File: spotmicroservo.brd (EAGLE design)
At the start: 25.4 x 39.4 mm, 39 parts, among them J1 B4B-PH-SM4-TB(LF)(SN), J2 CON_HEADER_1X02-B2B-XH-A(LF)(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

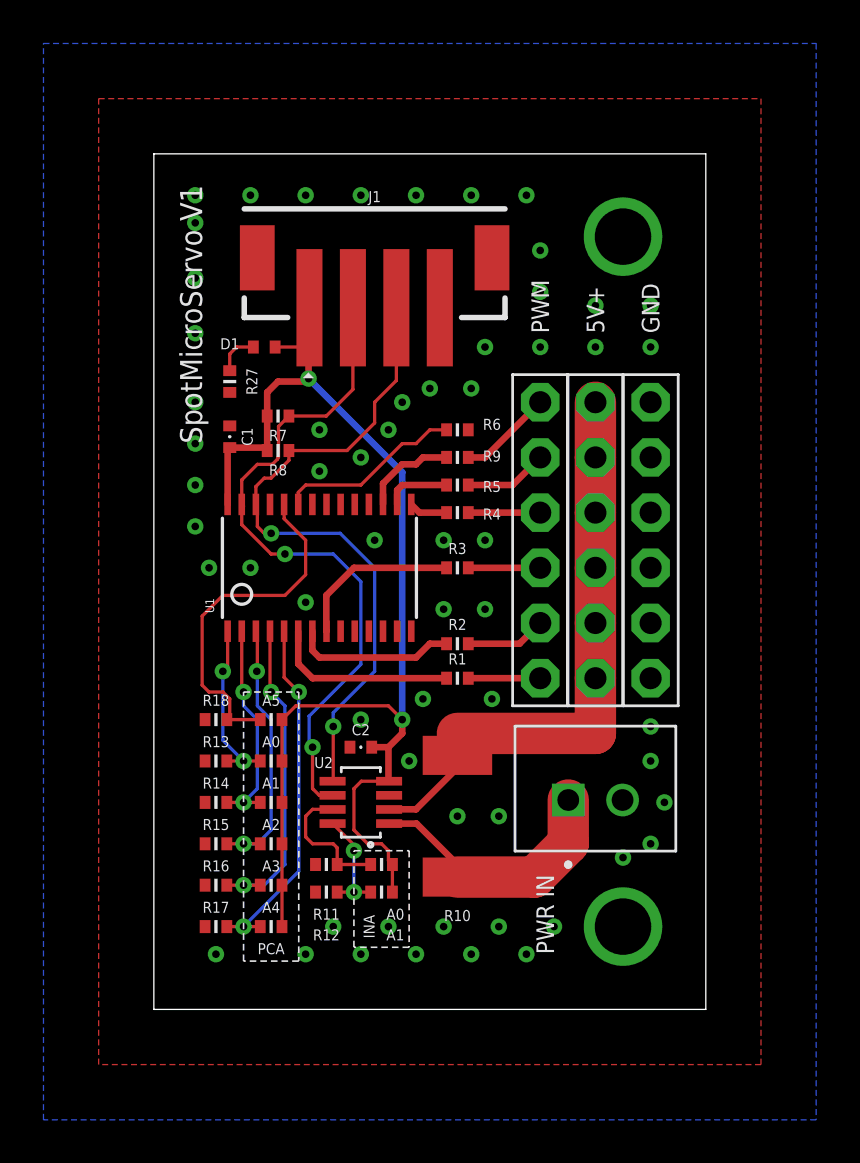
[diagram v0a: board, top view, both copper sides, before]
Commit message: Smaller vias. Prettify power path.
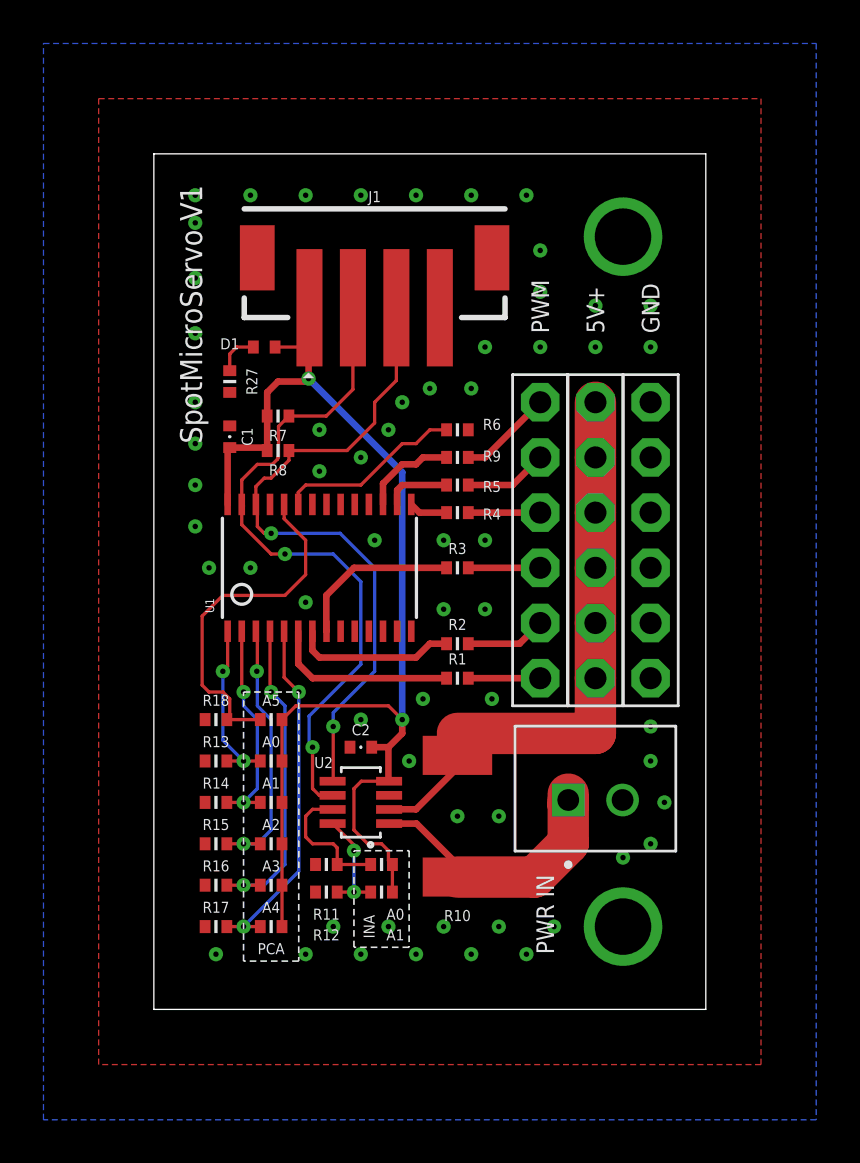
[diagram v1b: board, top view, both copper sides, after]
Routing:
- net VIN: track 12.2 -> 13.0 mm
